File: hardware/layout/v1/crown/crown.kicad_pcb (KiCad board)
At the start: 4 copper layers, 60 x 60 mm, 95 parts, among them J1 Main board, J10 DOME_SOCKET, J11 AUX 12V_HEAT, J12 SWD, J2 XD_N, J3 XD_E, J4 XD_S, J5 XD_W, J6 PIEZO_NE, J7 PIEZO_NW, J8 PIEZO_SW, J9 PIEZO_SE, U1 STM32G431RBT6, U10 XC6206P332MR, U2 UCC27524ADR, U3 UCC27524ADR, U4 UCC27524ADR, U5 UCC27524ADR, U6 MMC5603NJ, U7 74HC4052D, U8 TLV9062IDR, U9 AS3935-BQFT, Y1 8MHz

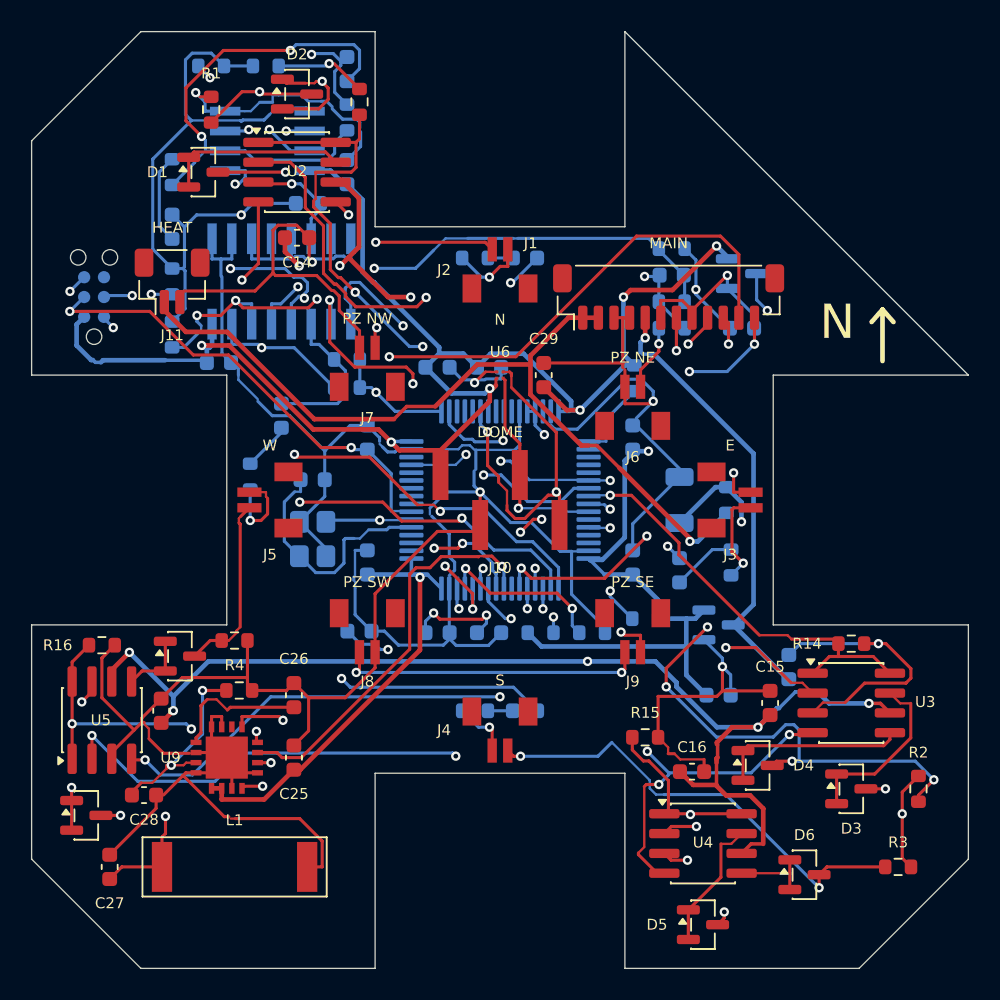
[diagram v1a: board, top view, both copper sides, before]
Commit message: Update dome PCB layout with manual reference and label placement, add Stock_Optional field for LTR-390UV-01 sensor to allow JLC assembly when in stock without failing release on shortage
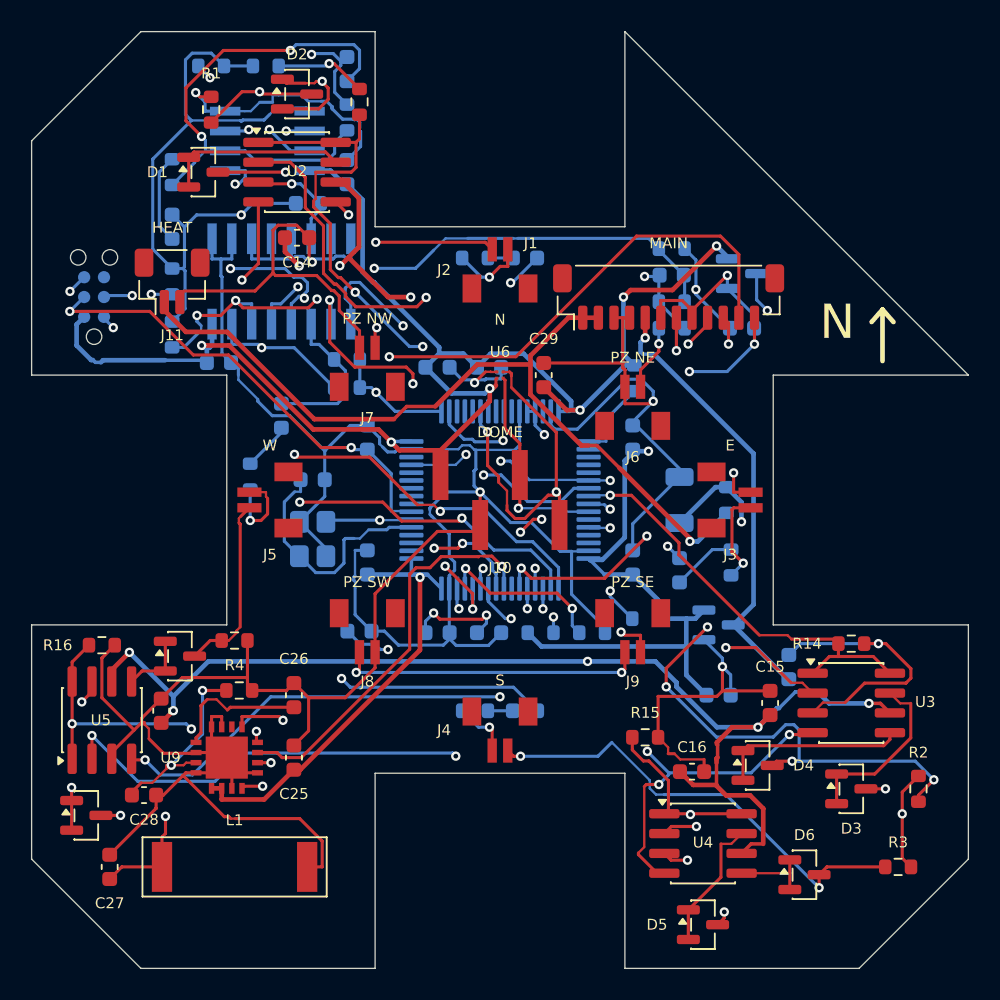
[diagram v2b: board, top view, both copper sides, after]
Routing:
- net GND: track 325.9 -> 335.4 mm

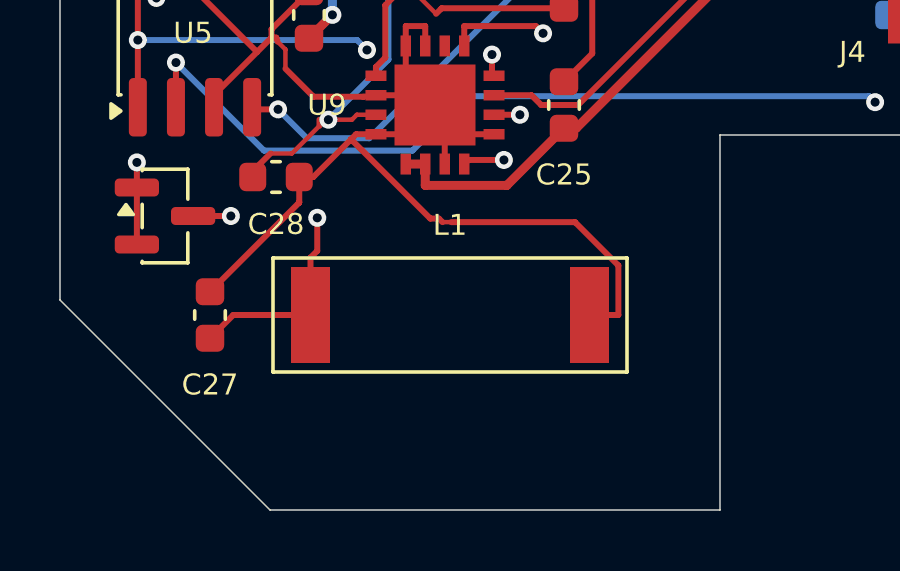
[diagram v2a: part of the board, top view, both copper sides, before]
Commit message: Update AS3935 lightning antenna to dual land pattern supporting Coilcraft MA5532-AE or Premo SDTR1103-HF1-0100J with adjusted Q damping resistor notes, and reorganize self-assembly order files to LCSC-only and elsewhere CSVs with multi-distributor columns
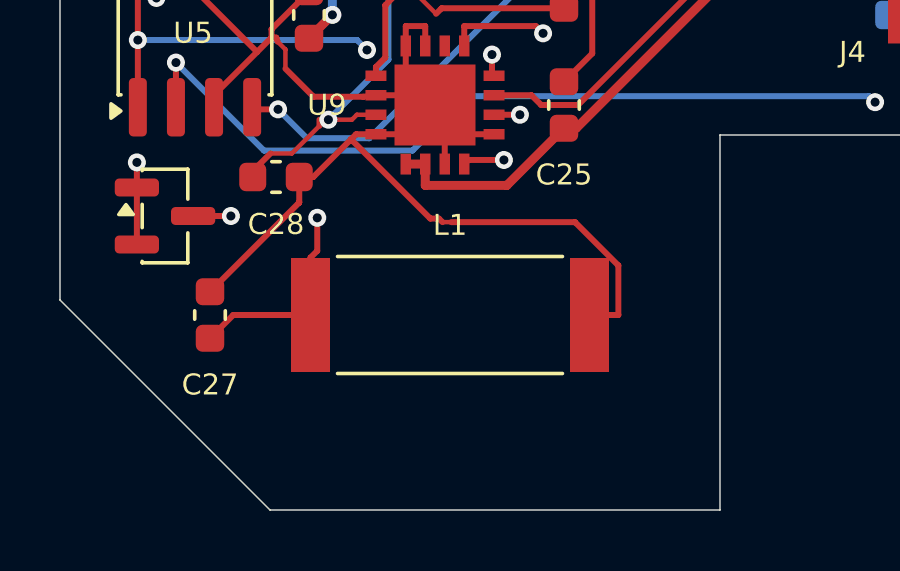
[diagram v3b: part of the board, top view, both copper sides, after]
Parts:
- L1: footprint RF_Antenna:Coilcraft_MA5532-AE_RFID -> gateway_fp:AS3935_Antenna_MA5532_SDTR1103
